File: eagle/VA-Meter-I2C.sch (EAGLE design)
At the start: 21 parts, among them IC1 MEGA328P, IC2 7805TV

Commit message: I2C-LCD 回路図を修正
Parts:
- removed R11: 1k, rcl:R-EU_0613/15
- added D2: 3.3V, diode:ZENER-DIODEZD-5
- added JP3: LCD-BL, pinhead:PINHD-1X2
- added R12: 1.5k, rcl:R-EU_0207/7
- added R13: 1k, rcl:R-EU_0207/7
- added R2: 220, rcl:R-EU_0207/7
- added R4: 470, rcl:R-EU_0207/7
- added R7: 1.2k, rcl:R-EU_0207/7
- added VR2: (no value), v-reg:TL431CLP
- R8: value 3.3k -> 100
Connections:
- removed net N$1: R11.1
- removed net N$16: C1.1, IC1.AVCC, L1.1
- new net +3V3: D2.C, JP1.1, R2.1
- new net N$5: C1.1, IC1.AVCC, L1.1, R13.2
- new net N$6: R12.2, R7.1, VR2.R
- new net N$7: IC1.AREF, R13.1, R7.2, VR2.C
- net -12V: no longer R11.2
- net N$2: now also JP3.2, R4.1; no longer JP1.4
- net V+: now also R2.2, R4.2; no longer JP1.1
- net V-: now also D2.A, JP1.4, JP3.1, R12.1, VR2.A
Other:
- moved on the sheet: C1, C3, L1

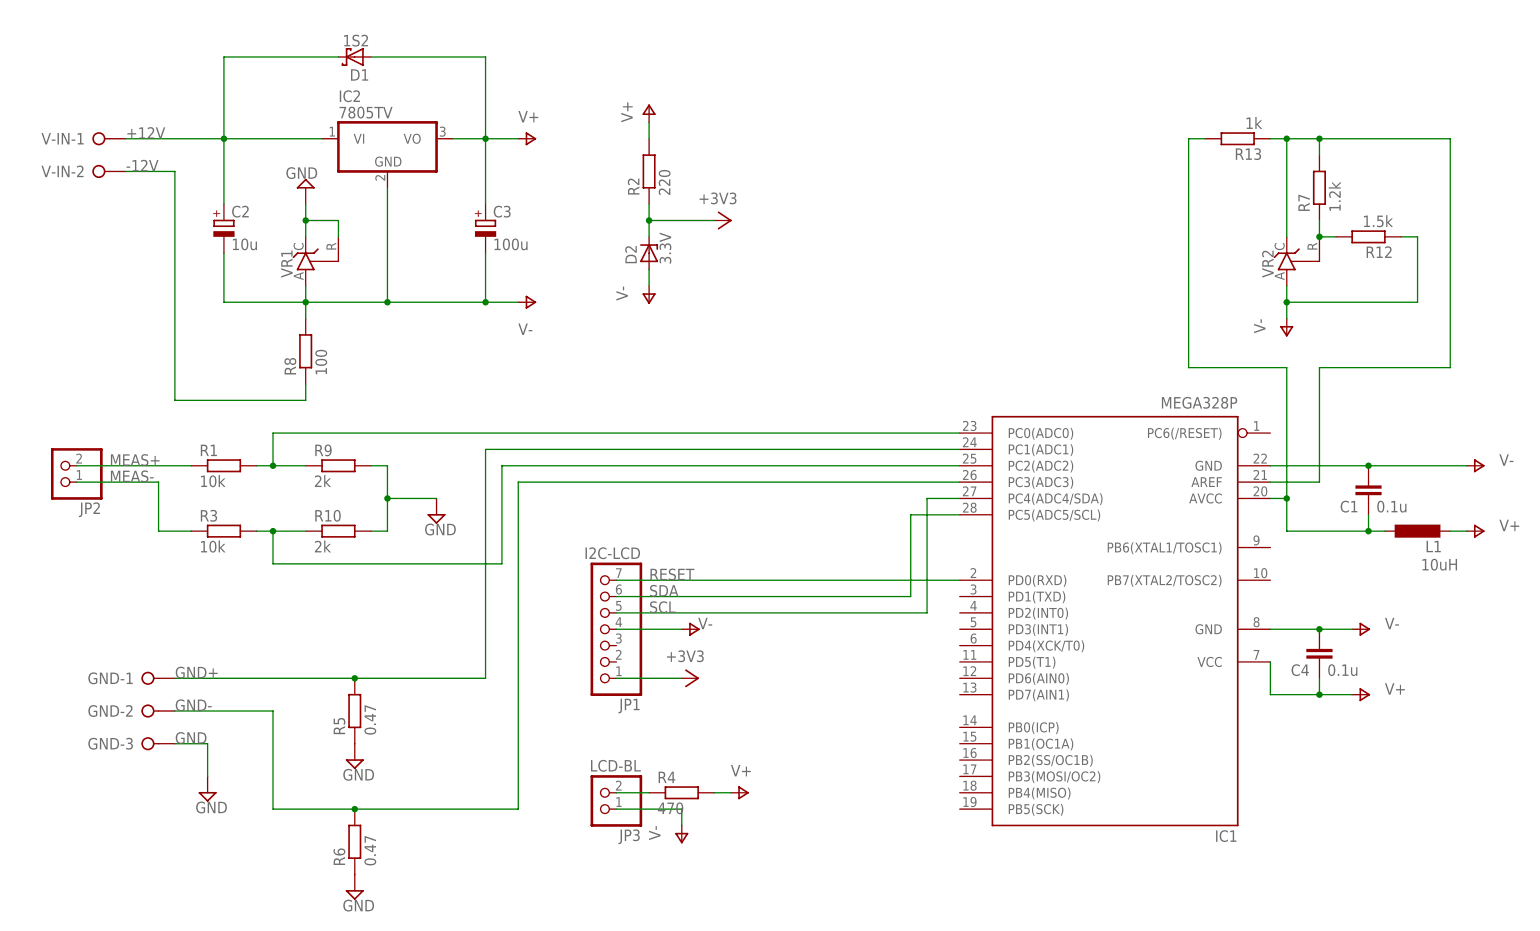
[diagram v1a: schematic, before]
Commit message: V-Meter-I2C 回路図修正 シャントレギュレータ－ではなくAVCCを基準電圧に
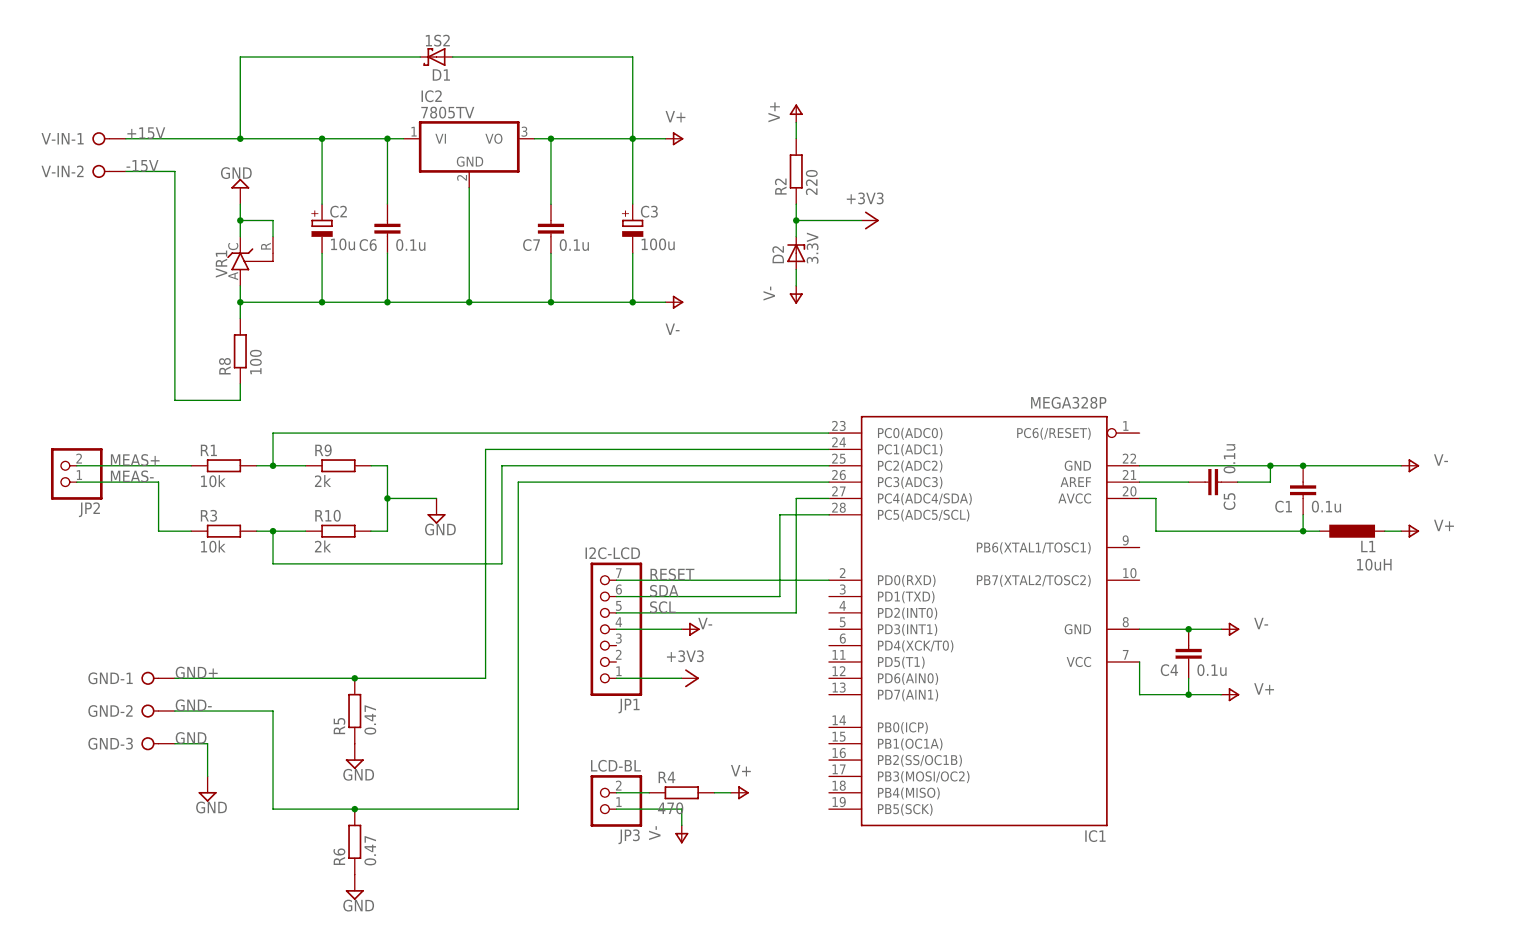
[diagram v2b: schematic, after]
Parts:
- removed R12: 1.5k, rcl:R-EU_0207/7
- removed R13: 1k, rcl:R-EU_0207/7
- removed R7: 1.2k, rcl:R-EU_0207/7
- removed VR2: (no value), v-reg:TL431CLP
- added C5, C6, C7: 0.1u, rcl:C-EU050-024X044
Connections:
- net -12V renamed -15V
- removed net +12V: C2.+, D1.C, IC2.VI, V-IN-1.KL
- removed net N$5: C1.1, IC1.AVCC, L1.1, R13.2
- removed net N$6: R12.2, R7.1, VR2.R
- removed net N$7: IC1.AREF, R13.1, R7.2, VR2.C
- new net +15V: C2.+, C6.2, D1.C, IC2.VI, V-IN-1.KL
- new net N$10: C1.1, IC1.AVCC, L1.1
- new net N$9: C5.2, IC1.AREF
- net V+: now also C7.2
- net V-: now also C5.1, C6.1, C7.1; no longer R12.1, VR2.A
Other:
- moved on the sheet: C1, C2, C3, C4, D1, D2, IC1, IC2, L1, R2, R8, VR1

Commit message: 電源部の保護回路を±のポリスイッチに変更
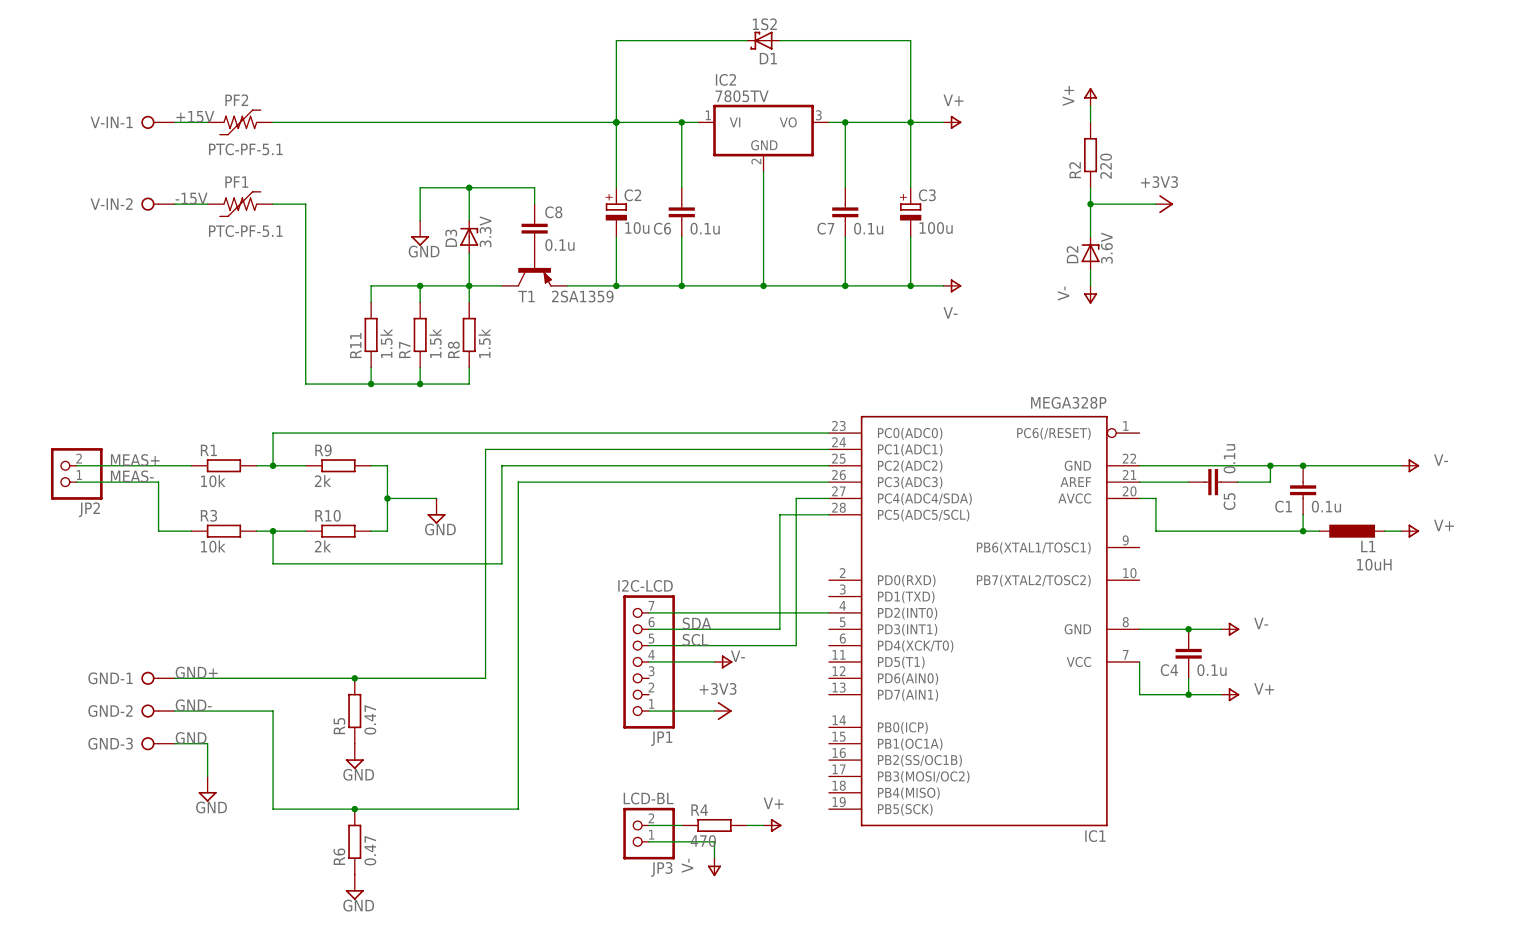
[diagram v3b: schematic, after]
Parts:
- removed VR1: (no value), v-reg:TL431CLP
- added C8: 0.1u, rcl:C-EU050-024X044
- added D3: 3.3V, diode:ZENER-DIODEZD-5
- added PF1, PF2: PTC-PF-5.1, polyswitch:PTC-PF-5.1
- added R11, R7: 1.5k, rcl:R-EU_0613/15
- added T1: 2SA1359, transistor:-PNP-TO126V
- D2: value 3.3V -> 3.6V
- R8: value 100 -> 1.5k
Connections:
- removed net RESET: IC1.PD0(RXD), JP1.7
- new net N$1: D3.A, R11.2, R7.2, R8.2, T1.C
- new net N$11: IC1.PD2(INT0), JP1.7
- new net N$5: C8.2, T1.B
- new net N$6: PF2.1, V-IN-1.KL
- new net N$7: PF1.1, V-IN-2.KL
- net +15V: now also PF2.2; no longer V-IN-1.KL
- net -15V: now also PF1.2, R11.1, R7.1; no longer V-IN-2.KL
- net GND: now also C8.1, D3.C; no longer VR1.C, VR1.R
- net V-: now also T1.E; no longer R8.2, VR1.A
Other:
- moved on the sheet: C2, C3, C6, C7, D1, D2, IC2, JP1, JP3, R2, R4, R8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
